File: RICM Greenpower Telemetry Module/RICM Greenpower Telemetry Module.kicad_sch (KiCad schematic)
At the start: 7 parts

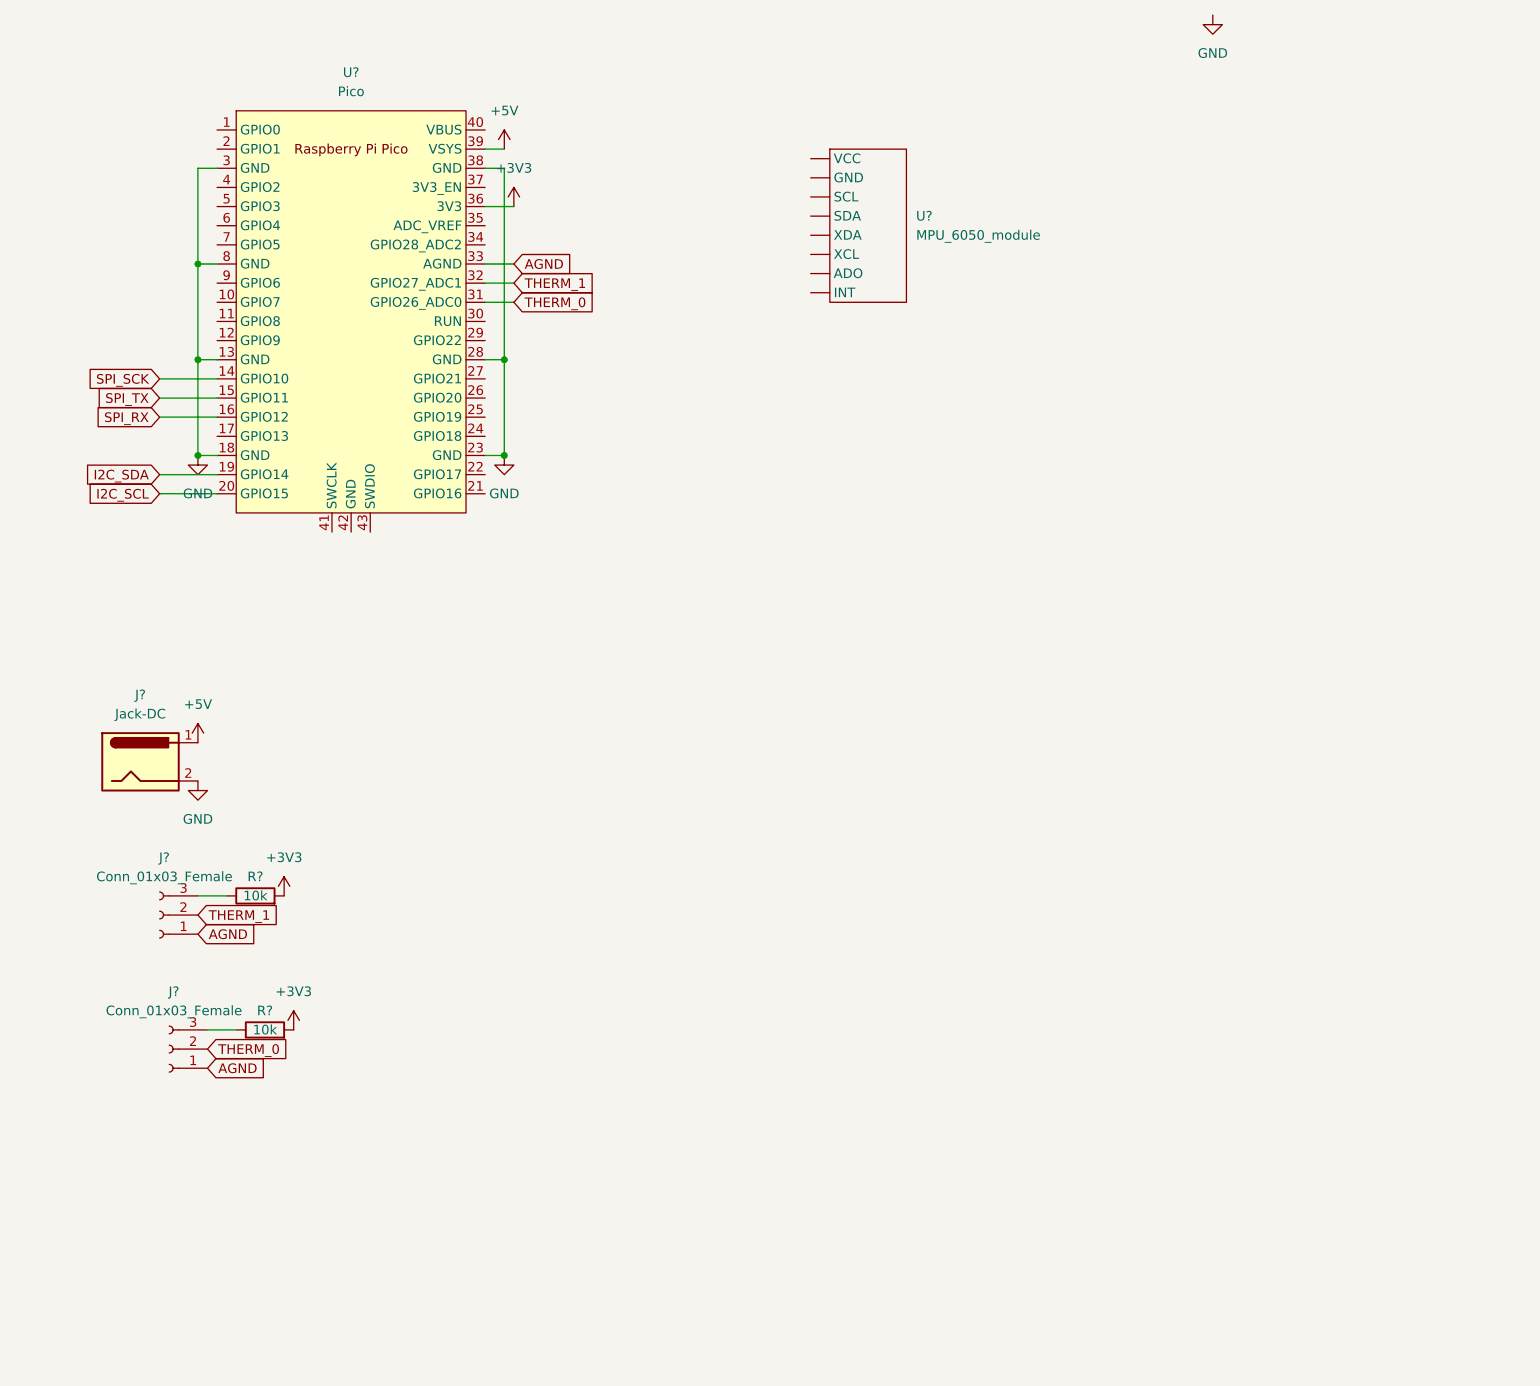
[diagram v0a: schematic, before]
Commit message: added most of the sensors we will probably want
3x temperature sensors
2x hall effect (for RPM)
2x battery voltage
1x current (inductive loop, 50A)
1x 3-axis gyro
1x 3-axis accelerometer
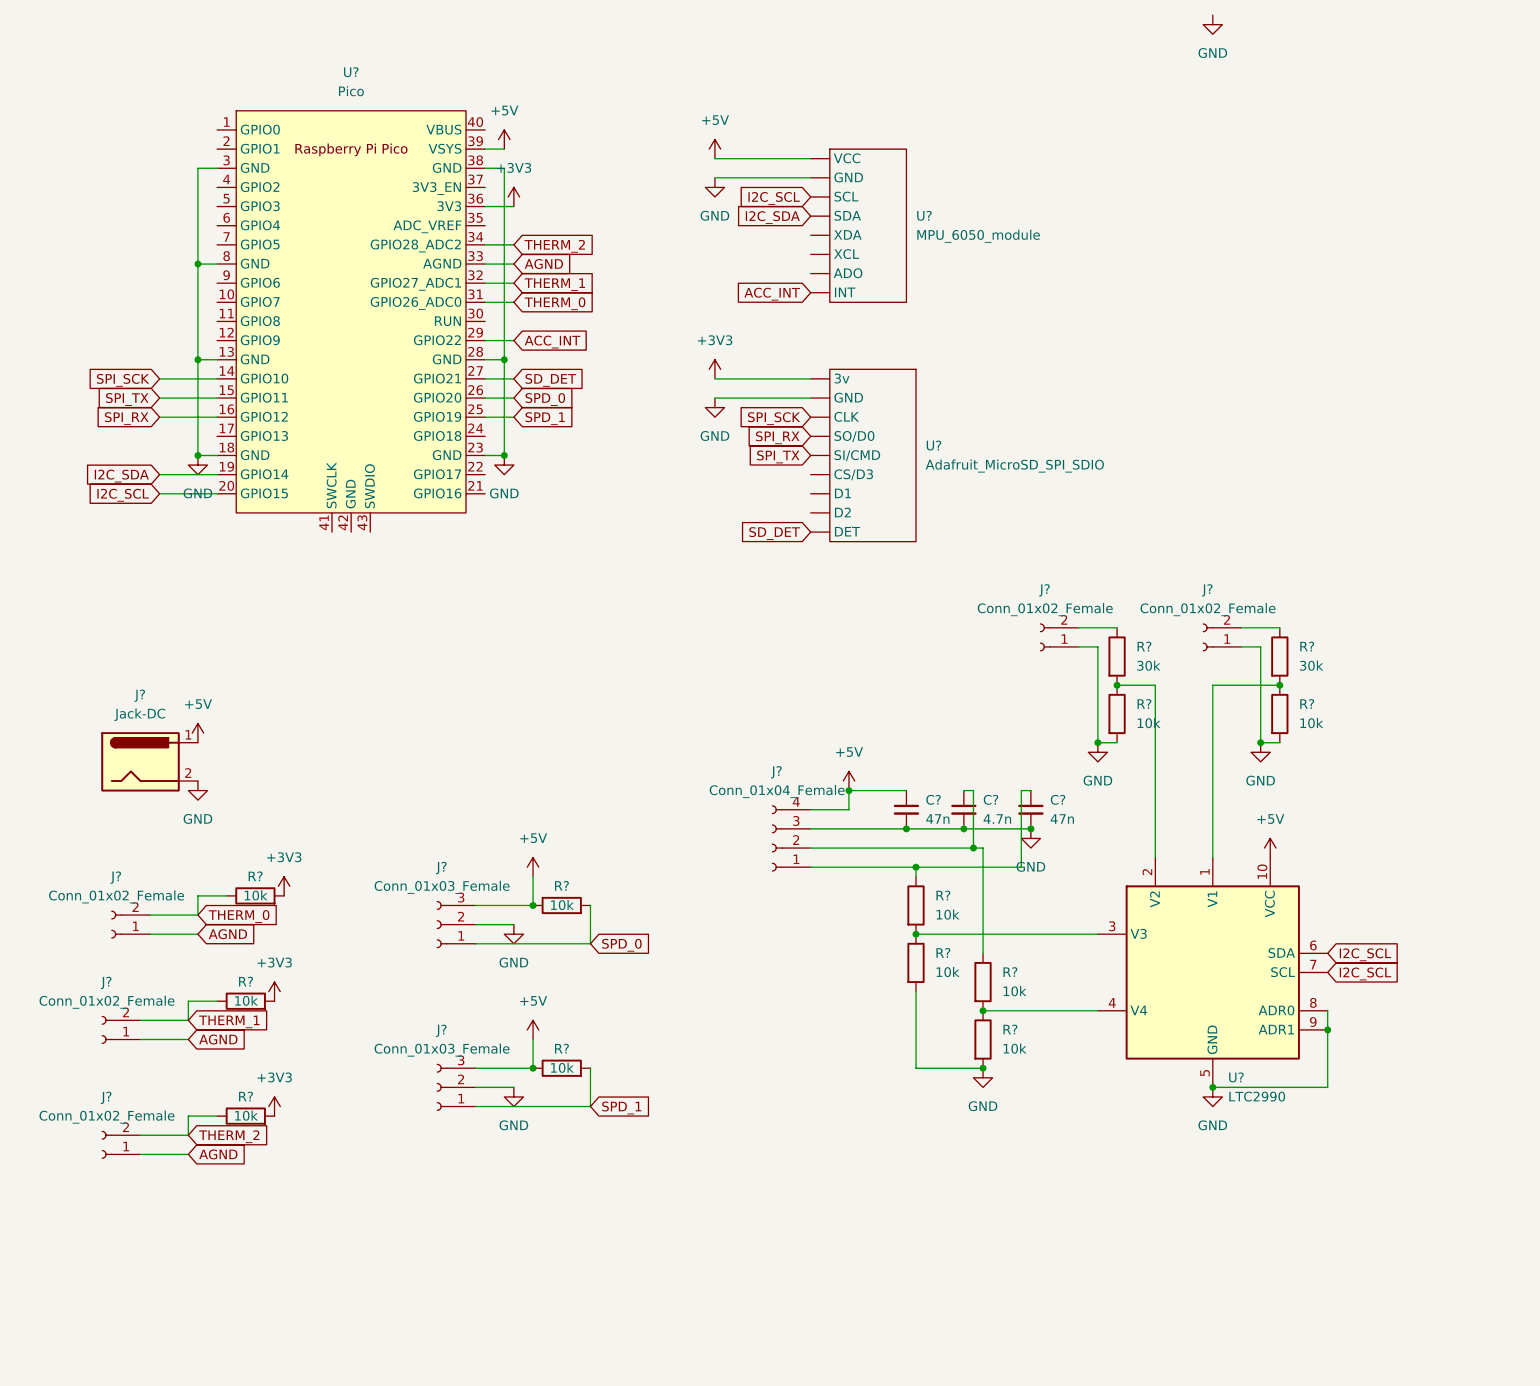
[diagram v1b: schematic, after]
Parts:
- removed J? (x2): Conn_01x03_Female, symbol Connector:Conn_01x03_Female
- removed R?: 10k, symbol Device:R
- added C? (x2): 47n, symbol Device:C_Small
- added C?: 4.7n, symbol Device:C_Small
- added J? (x5): Conn_01x02_Female, symbol Connector:Conn_01x02_Female
- added J?: Conn_01x04_Female, symbol Connector:Conn_01x04_Female
- added J? (x2): Conn_01x03_Female, symbol Connector:Conn_01x03_Female
- added R? (x10): 10k, symbol Device:R
- added R? (x2): 30k, symbol Device:R
- added U?: LTC2990, Package_SO:MSOP-10_3x3mm_P0.5mm, symbol Sensor:LTC2990
- added U?: Adafruit_MicroSD_SPI_SDIO, symbol Memory_Flash:Adafruit_MicroSD_SPI_SDIO
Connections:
- net +3V3: now also R?.2, R?.2, U?. (SO/D0)
- net +5V: now also U?. (XDA), C?.1, J?.3 (Pin_3), J?.3 (Pin_3), J?.4 (Pin_4), R?.1, R?.1, U?.10 (VCC)
- net AGND: now also J?.1 (Pin_1), J?.1 (Pin_1), J?.1 (Pin_1)
- net GND: now also U?. (XDA), C?.2, C?.2, C?.2, J?.1 (Pin_1), J?.1 (Pin_1), J?.2 (Pin_2), J?.2 (Pin_2), J?.3 (Pin_3), R?.2, R?.2, R?.2, R?.2, U?. (SO/D0), U?.5 (GND), U?.8 (ADR0), U?.9 (ADR1)
- net I2C_SCL: now also U?. (XDA), U?.6 (SDA), U?.7 (SCL)
- net I2C_SDA: now also U?. (XDA)
- net SPI_RX: now also U?. (SO/D0)
- net SPI_SCK: now also U?. (SO/D0)
- net SPI_TX: now also U?. (SO/D0)
- net THERM_0: now also R?.1, J?.2 (Pin_2)
- net THERM_1: now also J?.2 (Pin_2), R?.1
- net SPD_1: now reaches U?.25 (GPIO19)
- net SPD_1: now also J?.1 (Pin_1), R?.2
- net SPD_0: now reaches U?.26 (GPIO20)
- net SPD_0: now also J?.1 (Pin_1), R?.2
- net SD_DET: now reaches U?.27 (GPIO21)
- net SD_DET: now also U?. (SO/D0)
- net ACC_INT: now reaches U?.29 (GPIO22)
- net ACC_INT: now also U?. (XDA)
- net THERM_2: now reaches U?.34 (GPIO28_ADC2)
- net THERM_2: now also J?.2 (Pin_2), R?.1
- new net: R?.1, R?.2, U?.1 (V1)
- new net: R?.1, R?.2, U?.2 (V2)
- new net: R?.1, R?.2, U?.3 (V3)
- new net: R?.1, R?.2, U?.4 (V4)
- new net: J?.2 (Pin_2), R?.1 (x2)
- new net: C?.1, J?.1 (Pin_1), R?.1
- new net: C?.1, J?.2 (Pin_2), R?.1

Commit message: added more sensors and connectors
Added all the sensors and connectors that will go on this board (for now). Next step, layout
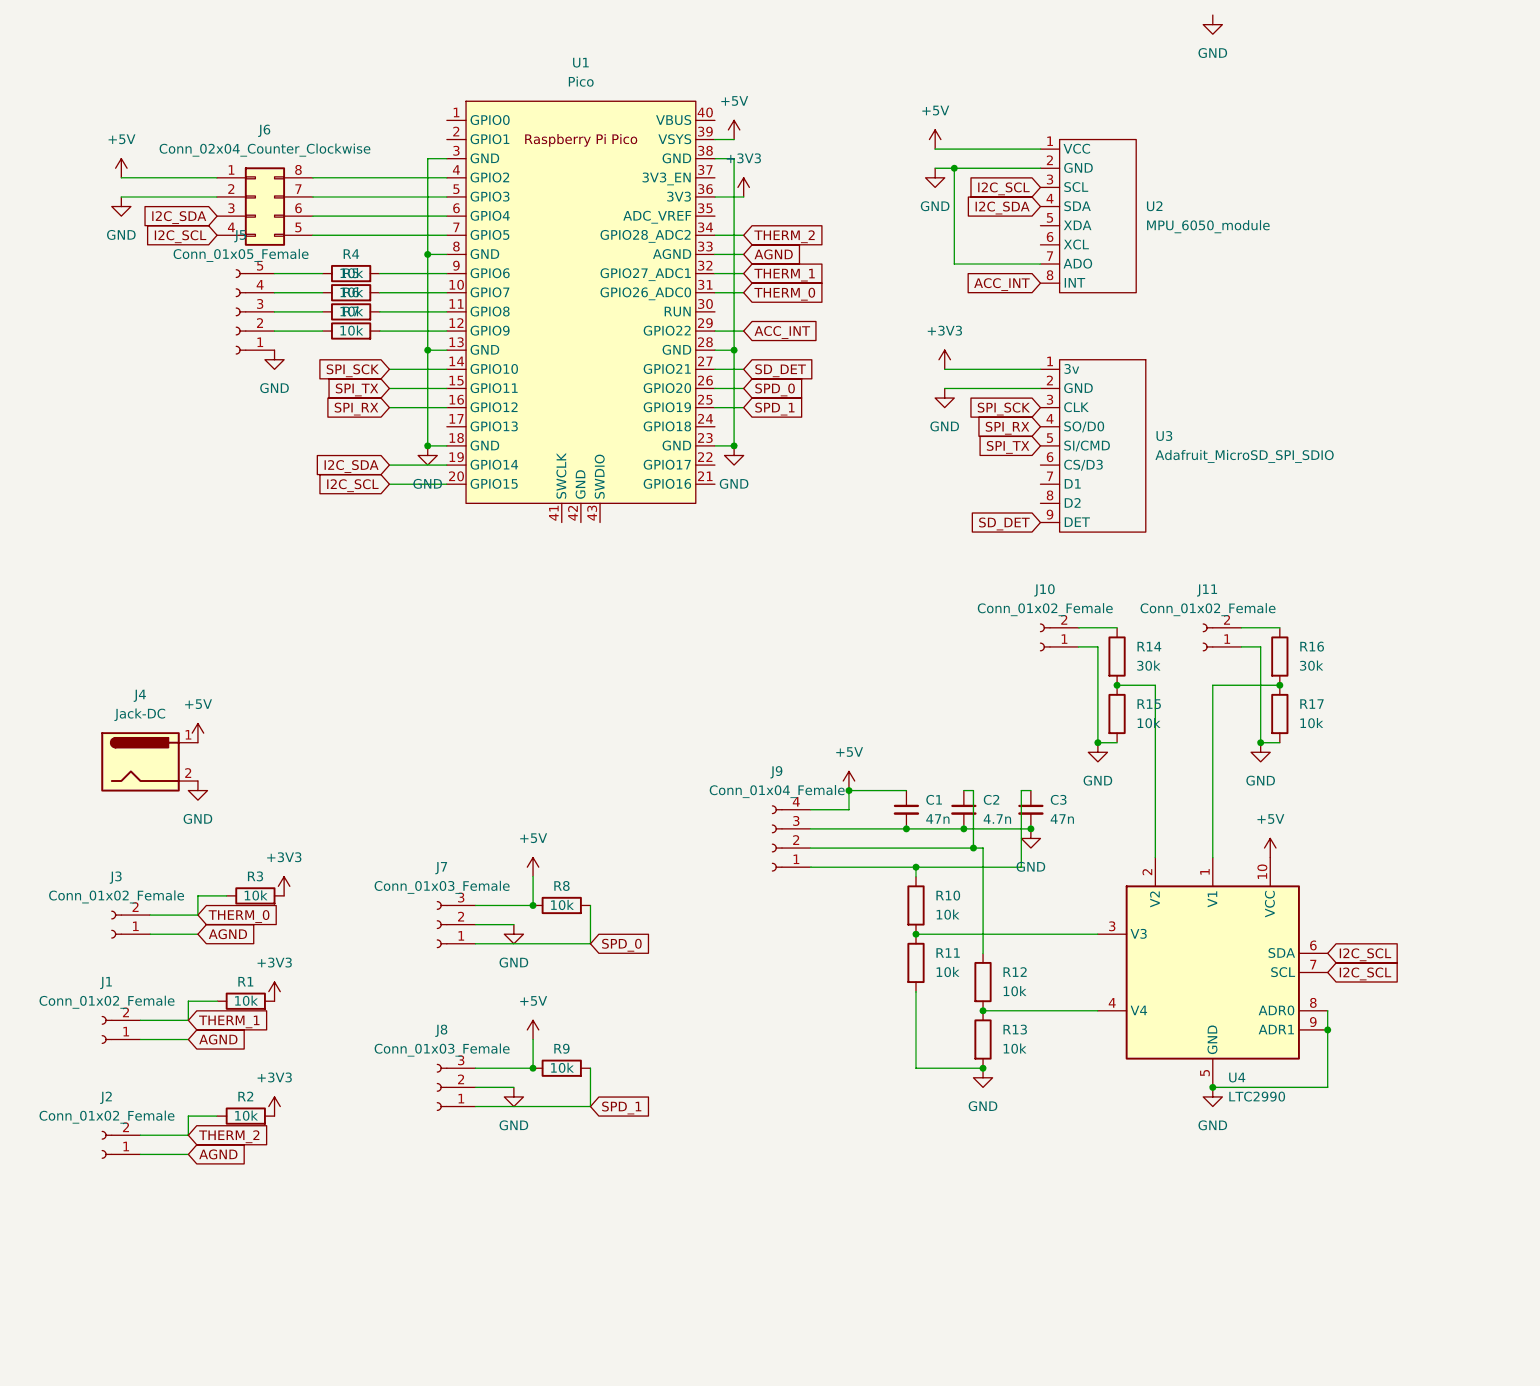
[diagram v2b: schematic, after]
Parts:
- added J5: Conn_01x05_Female, Connector_PinHeader_2.54mm:PinHeader_1x05_P2.54mm_Vertical, symbol Connector:Conn_01x05_Female
- added J6: Conn_02x04_Counter_Clockwise, Connector_PinHeader_2.54mm:PinHeader_2x04_P2.54mm_Vertical, symbol Connector_Generic:Conn_02x04_Counter_Clockwise
- added R4, R5, R6, R7: 10k, Resistor_THT:R_Axial_DIN0207_L6.3mm_D2.5mm_P7.62mm_Horizontal, symbol Device:R
- C1, C2, C3: renamed from C?; footprint (none) -> Capacitor_THT:C_Disc_D7.5mm_W5.0mm_P5.00mm
- J1, J10, J11, J2, J3: renamed from J?; footprint (none) -> Connector_PinHeader_2.54mm:PinHeader_1x02_P2.54mm_Vertical
- J4: renamed from J?; footprint (none) -> Connector_BarrelJack:BarrelJack_GCT_DCJ200-10-A_Horizontal
- J7, J8: renamed from J?; footprint (none) -> Connector_PinHeader_2.54mm:PinHeader_1x03_P2.54mm_Vertical
- J9: renamed from J?; footprint (none) -> Connector_PinHeader_2.54mm:PinHeader_1x04_P2.54mm_Vertical
- R1, R10, R11, R12, R13, R14, R15, R16, R17, R2, R3, R8, R9: renamed from R?; footprint (none) -> Resistor_THT:R_Axial_DIN0207_L6.3mm_D2.5mm_P7.62mm_Horizontal
- U1: renamed from U?; footprint RPi_Pico:RPi_Pico_SMD_TH -> Module:RPi_Pico_SMD_TH
- U2: renamed from U?; footprint (none) -> Module:MPU_6050_module
- U3: renamed from U?; footprint (none) -> Module:Adafruit_MicroSD_breakout
- gave numbers to parts that had none: 1
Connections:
- net +3V3: now also U3.1 (3v); no longer U3. (SO/D0)
- net +5V: now also U2.1 (VCC), J6.1 (Pin_1); no longer U2. (XDA)
- net ACC_INT: now also U2.8 (INT); no longer U2. (XDA)
- net GND: now also U2.2 (GND), U2.7 (ADO), U3.2 (GND), J5.1 (Pin_1), J6.2 (Pin_2); no longer U2. (XDA), U3. (SO/D0)
- net I2C_SCL: now also U2.3 (SCL), J6.4 (Pin_4); no longer U2. (XDA)
- net I2C_SDA: now also U2.4 (SDA), J6.3 (Pin_3); no longer U2. (XDA)
- net SD_DET: now also U3.9 (DET); no longer U3. (SO/D0)
- net SPI_RX: now also U3.4 (SO/D0); no longer U3. (SO/D0)
- net SPI_SCK: now also U3.3 (CLK); no longer U3. (SO/D0)
- net SPI_TX: now also U3.5 (SI/CMD); no longer U3. (SO/D0)
- net at U1.10 (GPIO7): now also R5.2
- net at U1.11 (GPIO8): now also R6.2
- net at U1.12 (GPIO9): now also R7.2
- net at U1.4 (GPIO2): now also J6.8 (Pin_8)
- net at U1.5 (GPIO3): now also J6.7 (Pin_7)
- net at U1.6 (GPIO4): now also J6.6 (Pin_6)
- net at U1.7 (GPIO5): now also J6.5 (Pin_5)
- net at U1.9 (GPIO6): now also R4.2
- new net: J5.2 (Pin_2), R7.1
- new net: J5.3 (Pin_3), R6.1
- new net: J5.4 (Pin_4), R5.1
- new net: J5.5 (Pin_5), R4.1
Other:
- moved on the sheet: U1
